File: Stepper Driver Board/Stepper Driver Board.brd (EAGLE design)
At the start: 36.8 x 21.6 mm, 24 parts, among them IC1 DRV8825PWP

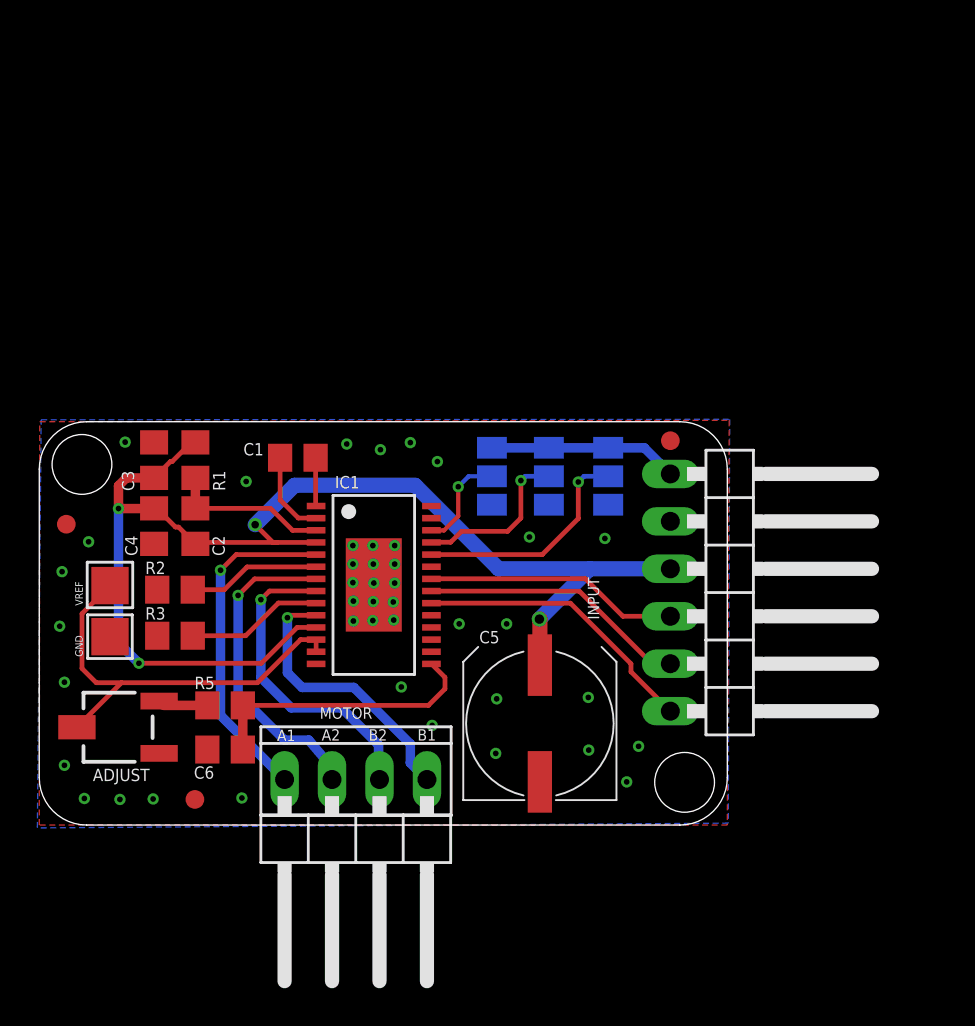
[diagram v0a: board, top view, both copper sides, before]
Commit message: The new REV_B has been shipped to production
New MainBoard Design, new Stepper drivers and new Extruder Board.
We also added many new components and configurations
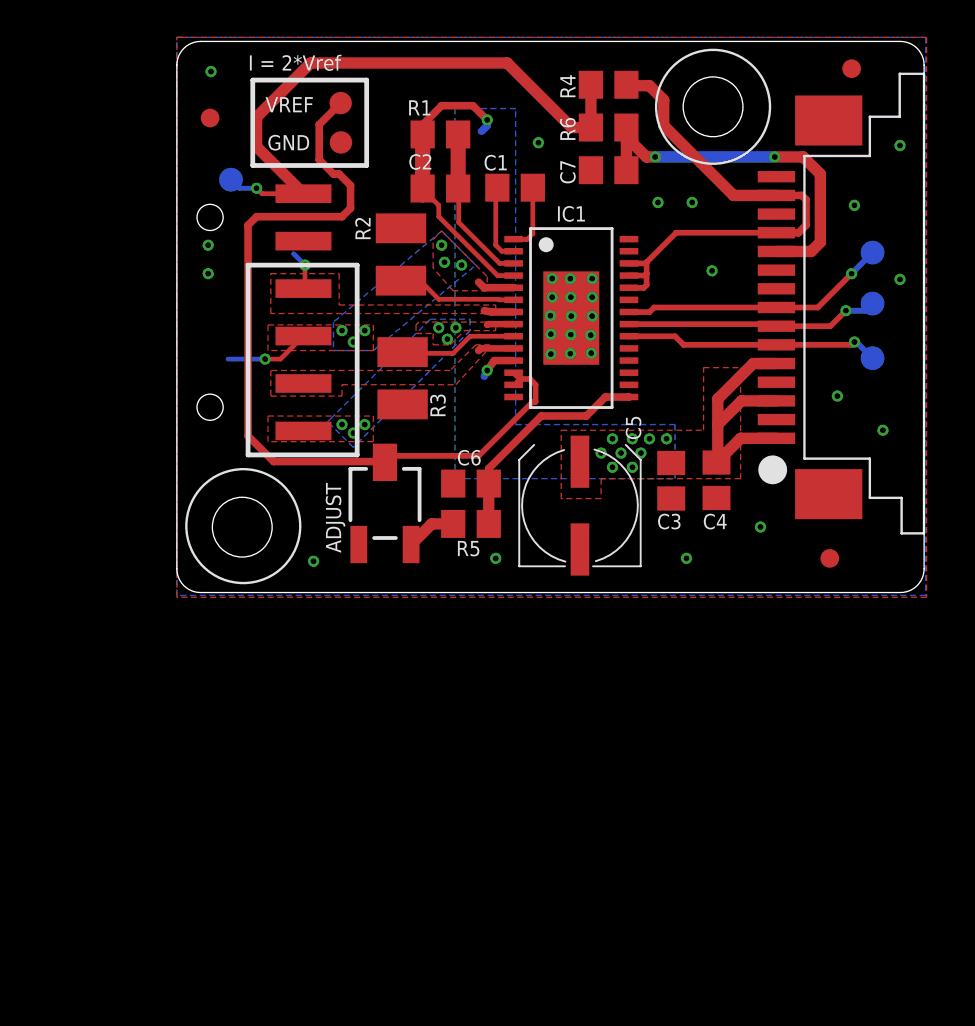
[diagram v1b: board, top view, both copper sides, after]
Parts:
- removed DRILEGEND: (no value), drilegend:DRILEGEND
- removed FID1, FID2, FID3: FIDUCIAL1X2, SparkFun-Aesthetics:FIDUCIAL-1X2
- removed INPUT: (no value), pinhead:1X06/90
- removed M0, M1, M2: (no value), jumper:SJ_2
- removed MOTOR: (no value), pinhead:1X04/90
- added C7: 0.1uF, rcl:C0805
- added FFC1: FFC_15V_90G_1MM, MarcEagleParts:TE_FFC_CON1MM
- added JP2: (no value), SparkFun-Connectors:1X06-SMD
- added R4: 4.7K, rcl:R0805
- added R6: 1K, rcl:R0805
- added TP1, TP2, TP3, TP8: TPB1,27, testpad:B1,27
- added U$1: (no value), MarcEagleParts:BCN3D_LOGO
- added U$2, U$3, U$4: FIDUCIAL, adafruit:FIDUCIAL_1MM
- added U$5: (no value), MarcEagleParts:FCIM_LOGO
- added U$6: (no value), MarcEagleParts:CC_LOGO
- C5: device rcl:UD-8X10_NICHICON -> rcl:UD-6,3X7,7_NICHICON
- GND, VREF: value TESTPAD_PTR1TP20SQ -> PTR1TP12R; device SAV MK-I:TESTPAD_TP20SQ -> testpad:TP12R
- R2, R3: device rcl:R0805 -> rcl:R1210
- moved LOGO1 38.7 mm to (30.0, 15.4)
- moved C4 30.2 mm to (28.9, 6.01)
- moved GND 29.2 mm to (8.78, 24.1), turned to 180 degrees
- moved VREF 28.6 mm to (8.77, 26.2)
- moved C3 27.7 mm to (26.5, 5.98), turned to 270 degrees
- moved C2 22.3 mm to (14.1, 21.6), turned to 180 degrees
- moved R1 21.8 mm to (14.1, 24.5), turned to 0 degrees
- moved R2 21.6 mm to (12.0, 18.1), turned to 90 degrees
- moved C6 19.4 mm to (15.7, 5.83)
- moved ADJUST 18.6 mm to (11.1, 4.77), turned to 90 degrees
- moved C1 18.6 mm to (18.1, 21.7)
- moved R3 18.4 mm to (12.1, 11.5), turned to 270 degrees
- moved IC1 17.8 mm to (21.1, 14.7)
- moved R5 16.4 mm to (15.7, 3.67)
- moved C5 11.9 mm to (21.6, 4.65)
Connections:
- removed net N$10: IC1.25, M1.2
- removed net N$13: IC1.26, M2.2
- removed net N$9: IC1.24, M0.2
- new net N$25: JP2.1, R4.1, R6.1, TP8.TP
- new net N$30: JP2.2
- new net STOP: C7.1, FFC1.11, R6.2
- net !EN: now also FFC1.7, TP3.TP; no longer INPUT.5
- net +24V: now also FFC1.1, FFC1.3, FFC1.5; no longer INPUT.3
- net +5V: now also FFC1.12, FFC1.14, IC1.24, IC1.25, IC1.26, R4.2; no longer INPUT.1, M0.3, M1.3, M2.3
- net A1: now also JP2.4; no longer MOTOR.4
- net A2: now also JP2.3; no longer MOTOR.3
- net B1: now also JP2.5; no longer MOTOR.1
- net B2: now also JP2.6; no longer MOTOR.2
- net DIR: now also FFC1.6, TP1.TP; no longer INPUT.6
- net GND: now also C7.2, FFC1.10, FFC1.13, FFC1.15, FFC1.2, FFC1.4, FFC1.9, FFC1.GND@1, FFC1.GND@2; no longer INPUT.2, M0.1, M1.1, M2.1
- net STEP: now also FFC1.8, TP2.TP; no longer INPUT.4
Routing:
- net +24V: track 70.0 -> 32.7 mm, vias 4 -> 11
- net N$25: track 0.00 -> 32.1 mm, vias 0 -> 1
- net VREF: track 22.9 -> 44.3 mm
- net STOP: track 0.00 -> 19.7 mm, vias 0 -> 2
- net +5V: track 10.1 -> 27.9 mm
- net B2: track 17.0 -> 1.43 mm, vias 1 -> 6
- net A2: track 17.2 -> 3.77 mm
- net B1: track 15.0 -> 1.92 mm, vias 1 -> 0
- net N$9: track 12.3 -> 0.00 mm, vias 1 -> 0
- net A1: track 18.1 -> 6.54 mm, vias 1 -> 7
- net N$10: track 8.93 -> 0.00 mm, vias 1 -> 0
- net N$13: track 5.36 -> 0.00 mm, vias 1 -> 0
- net +3V3: track 15.2 -> 12.1 mm
- net DIR: track 15.4 -> 13.7 mm, vias 0 -> 1
- net N$11: track 2.59 -> 3.63 mm
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- added copper zone on layer 1, net +24V
- added copper zone on layer 16, net +24V
- added copper zone on layer 1, net A1
- added copper zone on layer 16, net A1
- added copper zone on layer 1, net A2
- added copper zone on layer 1, net B1
- added copper zone on layer 1, net B2
- added copper zone on layer 16, net B2
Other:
- board size 36.8 x 21.6 mm -> 40 x 29.5 mm
- board text added: "BCN3D Electronics Stepper Driver Board v1.0 Designed in Barcelona ___________________ Stepper Driver - Jan 2015 Marc Cobler - REV_B ___________________"
- board text added: "I = 2*Vref"
- board text removed: "!EN"
- board text removed: "+24V"
- board text removed: "+5V"
- board text removed: "A1"
- board text removed: "A2"
- board text removed: "B1"
- board text removed: "B2"
- board text removed: "DIR"
- board text removed: "GND"
- board text removed: "LAYER-STACK"
- board text removed: "RepRapBCN Designed in Barcelona ------------------------------ Stepper Driver Board Marc Cobler Rev_A reprapbcn.com"
- board text removed: "STEP"

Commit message: BCN3D Electronics REV.E tested and manufactured
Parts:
- removed FFC1: FFC_15V_90G_1MM, MarcEagleParts:TE_FFC_CON1MM
- removed GND, VREF: PTR1TP12R, testpad:TP12R
- removed JP2: (no value), SparkFun-Connectors:1X06-SMD
- removed LOGO1: OSHW-LOGOL, SparkFun-Aesthetics:OSHW-LOGO-L
- removed TP1, TP2, TP3, TP8: TPB1,27, testpad:B1,27
- removed U$1: (no value), MarcEagleParts:BCN3D_LOGO
- removed U$6: (no value), MarcEagleParts:CC_LOGO
- added !EN, DIR, STEP, STOP: TPB1,27, testpad:B1,27
- added C8: 0.1uF, rcl:C0805
- added FFC2: FFC_15V_90G_1MM, MarcEagleParts:TE_FFC_CON1MM
- added MOTOR: (no value), MarcEagleParts:JST-6-PTH
- added SMAEX: (no value), SparkFun-Connectors:1X03
- added STOP1: (no value), adafruit:JST-PH-2-THM-RA
- added USTEP: (no value), jumper:SJ_2
- C3: value 0.1uF -> 100n
- moved R4 25.3 mm to (15.4, 3.10), turned to 270 degrees
- moved U$3 25.0 mm to (9.55, 1.63)
- moved R6 22.4 mm to (17.7, 3.10), turned to 270 degrees
- moved C5 20.6 mm to (19.0, 25.1), turned to 270 degrees
- moved C7 19.8 mm to (20.0, 3.10), turned to 90 degrees
- moved C3 18.8 mm to (24.3, 24.6), turned to 90 degrees
- moved ADJUST 18.4 mm to (29.5, 3.98), turned to 180 degrees
- moved C4 18.1 mm to (10.9, 7.53)
- moved R5 14.7 mm to (29.5, 8.83), turned to 90 degrees
- moved U$5 12.7 mm to (39.8, 0.76)
- moved C6 11.8 mm to (27.1, 8.81), turned to 270 degrees
- moved U$4 8.97 mm to (27.3, 26.5)
- moved U$2 3.05 mm to (38.0, 1.68)
- moved R1 2.75 mm to (13.2, 21.9)
- moved R2 2.21 mm to (10.6, 16.4), turned to 180 degrees
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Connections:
- removed net N$30: JP2.2
- new net N$4: IC1.24, USTEP.2
- net !EN: now also !EN.TP, FFC2.9; no longer FFC1.7, TP3.TP
- net +24V: now also C8.1, FFC2.11, FFC2.13, FFC2.15; no longer FFC1.1, FFC1.3, FFC1.5
- net +5V: now also FFC2.2, FFC2.4, IC1.16, IC1.17, SMAEX.1, USTEP.3; no longer FFC1.12, FFC1.14, IC1.24, IC1.25
- net A1: now also MOTOR.6; no longer JP2.4
- net A2: now also MOTOR.4; no longer JP2.3
- net B1: now also MOTOR.1; no longer JP2.5
- net B2: now also MOTOR.3; no longer JP2.6
- net DIR: now also DIR.TP, FFC2.7; no longer FFC1.6, TP1.TP
- net GND: now also C8.2, FFC2.1, FFC2.12, FFC2.14, FFC2.3, FFC2.6, FFC2.8, FFC2.GND@1, FFC2.GND@2, IC1.25, MOTOR.2, MOTOR.5, SMAEX.2, STOP1.1, USTEP.1; no longer FFC1.10, FFC1.13, FFC1.15, FFC1.2, FFC1.4, FFC1.9, FFC1.GND@1, FFC1.GND@2, GND.TP
- net N$25: now also STOP1.2; no longer JP2.1, TP8.TP
- net STEP: now also FFC2.10, STEP.TP; no longer FFC1.8, TP2.TP
- net STOP: now also FFC2.5, SMAEX.3, STOP.TP; no longer FFC1.11
- net VREF: no longer VREF.TP
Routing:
- net +5V: track 27.9 -> 107.0 mm, vias 0 -> 3
- net STOP: track 19.7 -> 74.2 mm, vias 2 -> 1
- net VREF: track 44.3 -> 15.1 mm
- net +24V: track 32.7 -> 44.0 mm, vias 11 -> 15
- net A2: track 3.77 -> 13.0 mm, vias 1 -> 3
- net B2: track 1.43 -> 9.98 mm, vias 6 -> 3
- net GND: track 0.00 -> 8.51 mm, vias 31 -> 74
- net B1: track 1.92 -> 10.3 mm, vias 0 -> 3
- net N$4: track 0.00 -> 7.51 mm, vias 0 -> 1
- net +3V3: track 12.1 -> 5.52 mm
- net A1: track 6.54 -> 12.5 mm, vias 7 -> 3
- net N$25: track 32.1 -> 37.5 mm, vias 1 -> 0
- net N$2: track 2.71 -> 4.37 mm
- net N$11: track 3.63 -> 2.56 mm
- net N$14: track 8.57 -> 7.67 mm
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- removed copper zone on layer 16, net A1
- removed copper zone on layer 16, net B2
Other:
- board text added: "+5v"
- board text added: "1/16"
- board text added: "1/32"
- board text added: "A1"
- board text added: "A2"
- board text added: "B1"
- board text added: "B2"
- board text added: "BCN3D Electronics Stepper Driver Board v1.0 Designed in Barcelona"
- board text added: "May 2015 REV_D"
- board text added: "gnd"
- board text added: "stop"
- board text removed: "BCN3D Electronics Stepper Driver Board v1.0 Designed in Barcelona ___________________ Stepper Driver - Jan 2015 Marc Cobler - REV_B ___________________"
- board text removed: "I = 2*Vref"
